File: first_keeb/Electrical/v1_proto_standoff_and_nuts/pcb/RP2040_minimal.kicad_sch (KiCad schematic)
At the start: 71 parts, among them J1 Conn_01x04_Socket, P1 USB-TYPE-C-016, Q1 BSS138, SW3 TS-1187A-B-A-B, SW5 TS-1187A-B-A-B, SW6 BUTT1, SW7 BUTT3, SW8 BUTT2, U1 ME6208A44M3G, U2 ME6206A25XG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

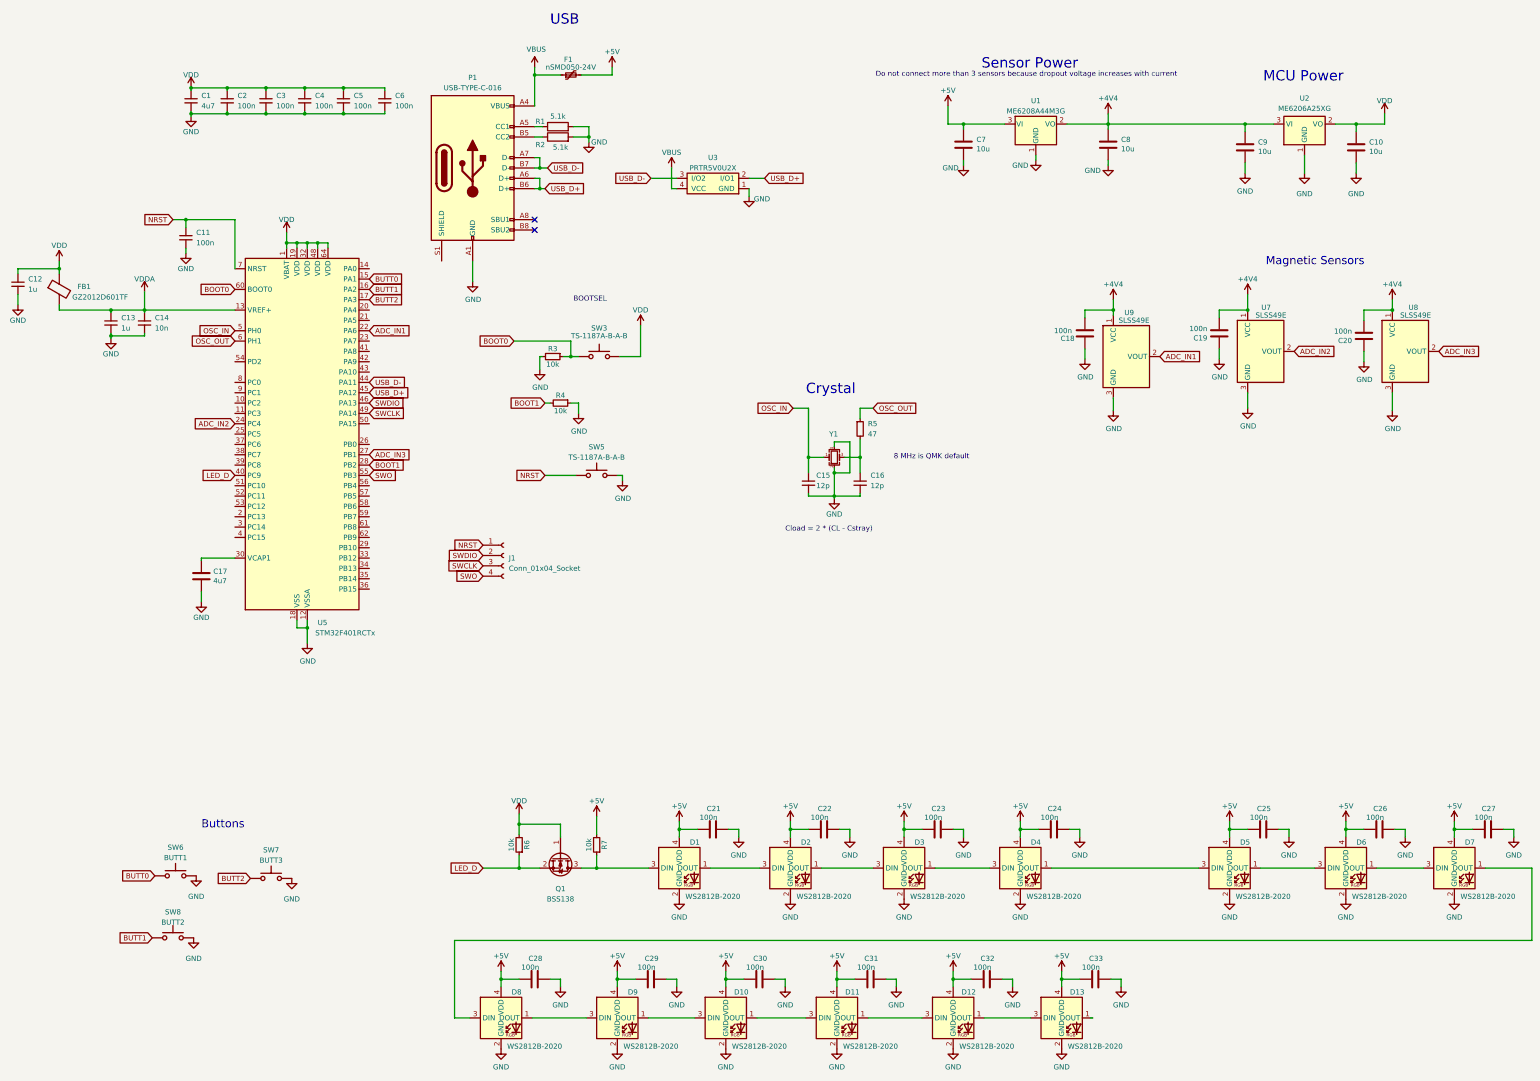
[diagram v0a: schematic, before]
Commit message: changes to ws2812b 5050 and moves 5v power rail to mostly 4th layer
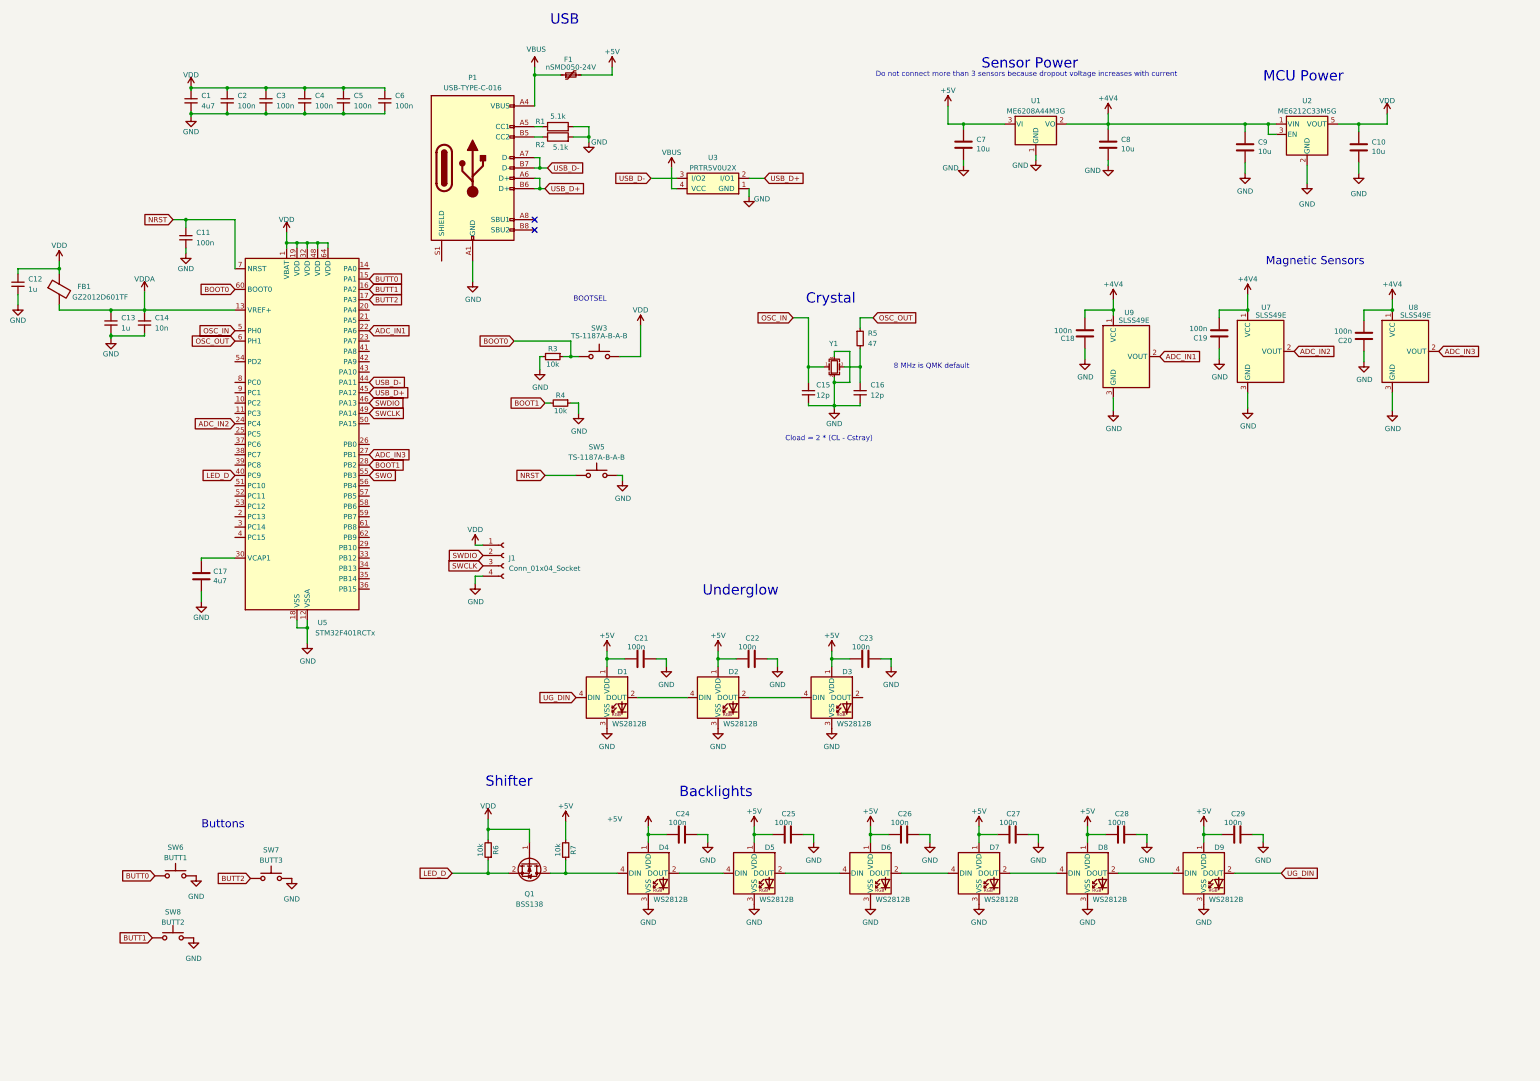
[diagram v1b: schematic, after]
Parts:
- removed C30, C31, C32, C33: 100n, Capacitor_SMD:C_0402_1005Metric, symbol Device:C
- removed D10, D11, D12, D13: WS2812B-2020, LED_SMD:LED_WS2812B-2020_PLCC4_2.0x2.0mm, symbol LED:WS2812B-2020
- removed U2: ME6206A25XG, Package_TO_SOT_SMD:SOT-23, symbol Regulator_Linear:AMS1117-2.5
- added U2: ME6212C33M5G, Package_TO_SOT_SMD:SOT-23-5, symbol Regulator_Linear:AP2127K-3.3
- D1, D2, D3, D4, D5, D6, D7, D8, D9: value WS2812B-2020 -> WS2812B; footprint LED_SMD:LED_WS2812B-2020_PLCC4_2.0x2.0mm -> LED_SMD:LED_WS2812B_PLCC4_5.0x5.0mm_P3.2mm; symbol LED:WS2812B-2020 -> LED:WS2812B
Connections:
- net +4V4: now also U2.1 (VIN), U2.3 (EN)
- net +5V: now also D1.1 (VDD), D2.1 (VDD), D3.1 (VDD), D4.1 (VDD), D5.1 (VDD), D6.1 (VDD), D7.1 (VDD), D8.1 (VDD), D9.1 (VDD); no longer D1.4 (VDD), D2.4 (VDD), D3.4 (VDD), D4.4 (VDD), D5.4 (VDD), D6.4 (VDD), D7.4 (VDD), D8.4 (VDD), D9.4 (VDD)
- net GND: now also D1.3 (VSS), D2.3 (VSS), D3.3 (VSS), D4.3 (VSS), D5.3 (VSS), D6.3 (VSS), D7.3 (VSS), D8.3 (VSS), D9.3 (VSS), J1.4 (Pin_4), U2.2 (GND); no longer D1.2 (GND), D2.2 (GND), D3.2 (GND), D4.2 (GND), D5.2 (GND), D6.2 (GND), D7.2 (GND), D8.2 (GND), D9.2 (GND)
- net NRST: no longer J1.1 (Pin_1)
- net SWO: no longer J1.4 (Pin_4)
- net VDD: now also J1.1 (Pin_1), U2.5 (VOUT)
- net at Q1.3 (D), R7.1: now also D4.4 (DIN); no longer D1.3 (DIN)
- new net: D1.2 (DOUT), D2.4 (DIN)
- new net: D8.2 (DOUT), D9.4 (DIN)
- new net: D7.2 (DOUT), D8.4 (DIN)
- new net: D2.2 (DOUT), D3.4 (DIN)
- new net: D6.2 (DOUT), D7.4 (DIN)
- new net: D4.2 (DOUT), D5.4 (DIN)
- new net: D5.2 (DOUT), D6.4 (DIN)
- new net UG_DIN: D1.4 (DIN), D9.2 (DOUT)
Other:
- note added: "Backlights"
- note added: "Shifter"
- note added: "Underglow"
- moved on the sheet: C10, C15, C16, C21, C22, C23, C24, C25, C26, C27, C28, C29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

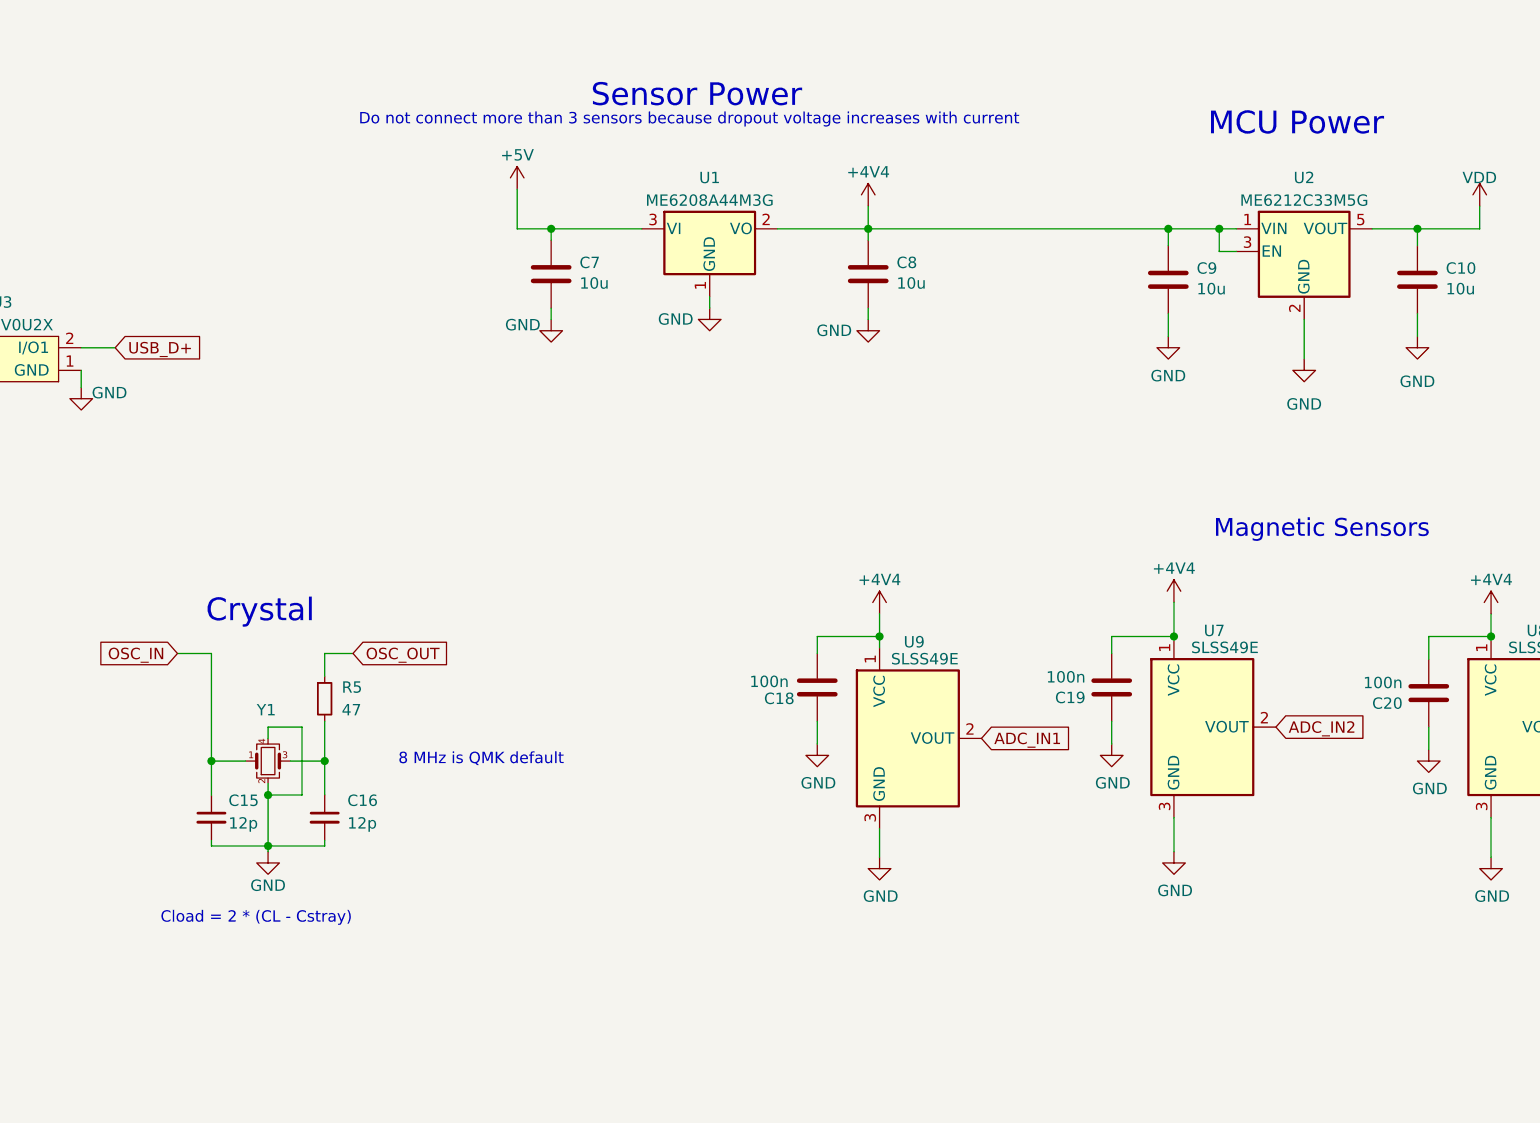
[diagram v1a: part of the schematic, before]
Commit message: v1 stm ordered
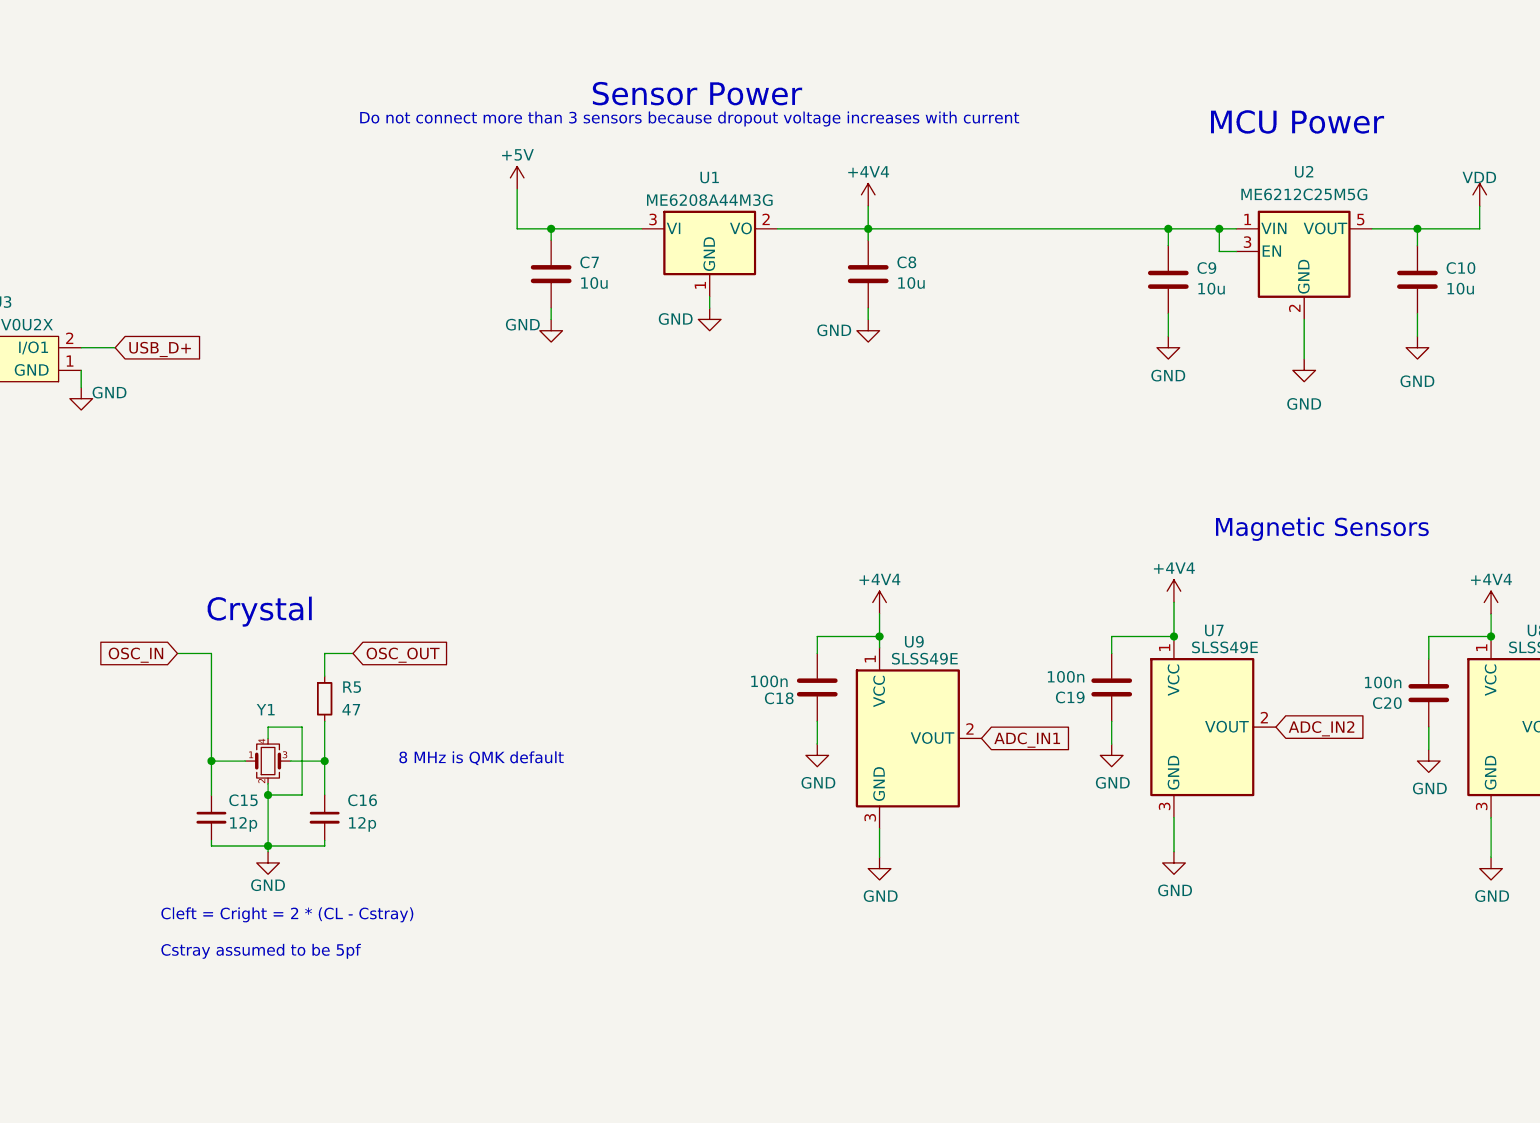
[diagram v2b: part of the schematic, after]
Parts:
- U2: value ME6212C33M5G -> ME6212C25M5G
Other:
- note added: "Cleft = Cright = 2 * (CL - Cstray) Cstray assumed to be 5pf"
- note removed: "Cload = 2 * (CL - Cstray)"
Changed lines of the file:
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@@
     (effects (font (size 2.54 2.54)) (justify left bottom))
   )
-  (text "Cload = 2 * (CL - Cstray)" (at 210.185 121.285 0)
+  (text "Cleft = Cright = 2 * (CL - Cstray)\n\nCstray assumed to be 5pf"
+    (at 210.185 125.095 0)
     (effects (font (size 1.27 1.27)) (justify left bottom))
   )
@@
   (symbol (lib_id "Regulator_Linear:AP2127K-3.3") (at 338.455 45.72 0) (unit 1)
     (in_bom yes) (on_board yes) (dnp no) (fields_autoplaced)
-    (property "Reference" "U2" (at 338.455 37.465 0)
-      (effects (font (size 1.27 1.27)))
-    )
-    (property "Value" "ME6212C33M5G" (at 338.455 40.005 0)
-      (effects (font (size 1.27 1.27)))
-    )
+    (property "Reference" "U2" (at 338.455 36.83 0)
+      (effects (font (size 1.27 1.27)))
+    )
+    (property "Value" "ME6212C25M5G" (at 338.455 39.37 0)
+      (effects (font (size 1.27 1.27)))
+    )
